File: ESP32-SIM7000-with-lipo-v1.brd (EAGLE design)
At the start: 90 x 60 mm, 72 parts, among them IC2 TXB0104, Q1 BSS138L, Q2 BSS138L, Q3 9013, Q5 9013, U3 ESP-WROOM-32, U4 MCP73831T-2ACI/OT, X1 LTE-uFL

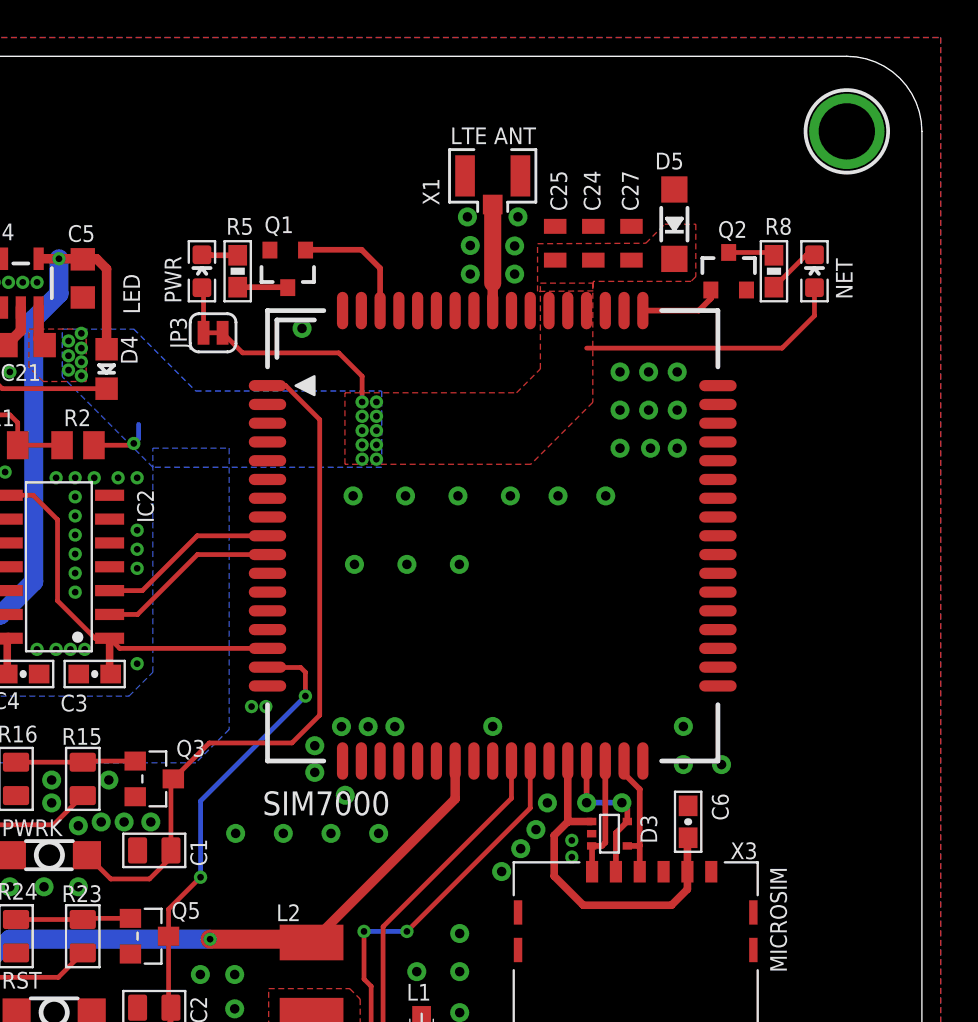
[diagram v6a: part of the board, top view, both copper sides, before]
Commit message: Adds power caps
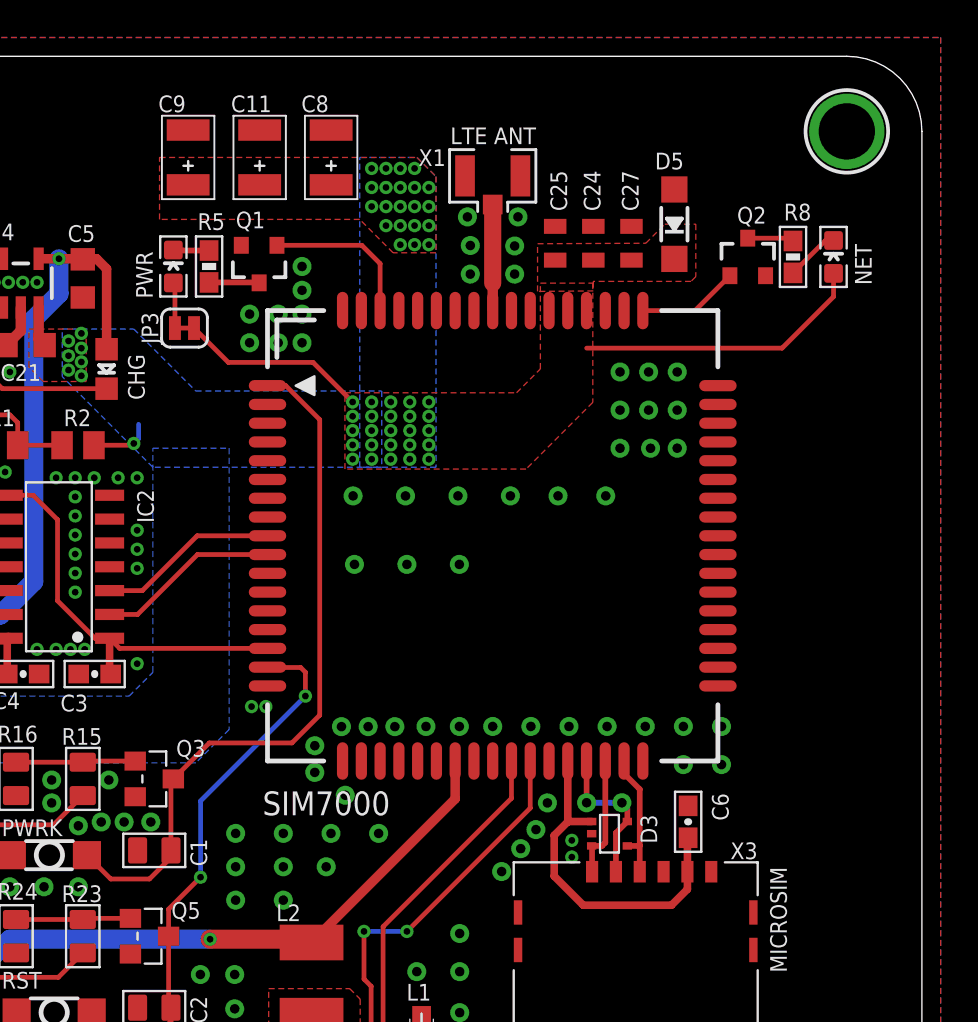
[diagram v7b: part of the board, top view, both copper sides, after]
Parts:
- added C11, C8, C9: 220uF/6.3V, discrete:AVX_B
- moved LED2 1.55 mm to (50.0, 48.8)
- moved R5 1.55 mm to (51.9, 48.8)
- moved JP3 1.55 mm to (50.6, 45.5)
- moved Q1 1.55 mm to (54.6, 48.9)
- moved LED3 1.27 mm to (85.2, 49.3)
- moved Q2 1.27 mm to (80.6, 49.3)
- moved R8 1.27 mm to (83.0, 49.3)
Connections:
- net +4.1V: now also C11.+, C8.+, C9.+
- net GND: now also C11.-, C8.-, C9.-
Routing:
- net PWR_STAT: track 6.64 -> 8.43 mm
- net +4.1V: track 32.2 -> 33.7 mm, vias 26 -> 62
- net NETLIGHT: track 4.35 -> 5.41 mm
- net GND: vias 157 -> 176
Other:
- board text added: "CHG"
- board text removed: "LED"

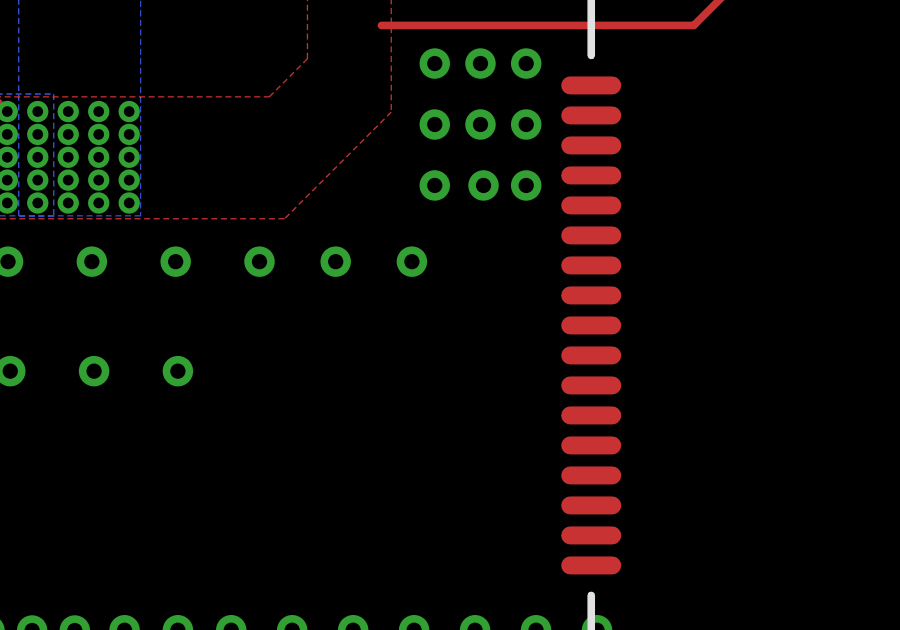
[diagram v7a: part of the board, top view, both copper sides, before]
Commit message: Adds some vias
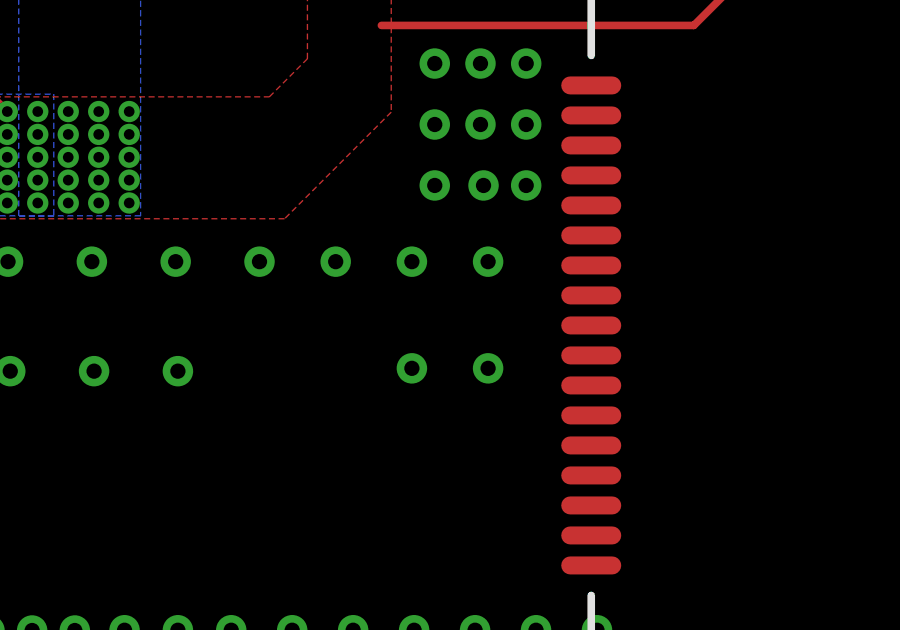
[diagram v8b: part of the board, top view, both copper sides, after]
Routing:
- net GND: vias 176 -> 179
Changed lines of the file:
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@@
 <via x="55.8708" y="15.0352" extent="1-16" drill="0.508" diameter="1.016"/>
 <via x="58.1568" y="16.8132" extent="1-16" drill="0.508" diameter="1.016"/>
+<via x="73.0504" y="33.02" extent="1-16" drill="0.508" diameter="1.016"/>
+<via x="75.5904" y="33.02" extent="1-16" drill="0.508" diameter="1.016"/>
+<via x="75.5904" y="36.576" extent="1-16" drill="0.508" diameter="1.016"/>
 </signal>
 <signal name="1.8V">
